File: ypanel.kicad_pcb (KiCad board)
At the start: 6 copper layers, 64 x 58 mm, 57 parts, among them IC2 TSL2561, J1 XF2M-1015-1A, J2 U.FL-R-SMT-1, J3 BATTERY CONNECTOR, J4 B2B-PH-SM4-TB_LF__SN_, U1 SWLP.12.B, U2 Value, U3 SW_SPDT, U4 SW_SPDT

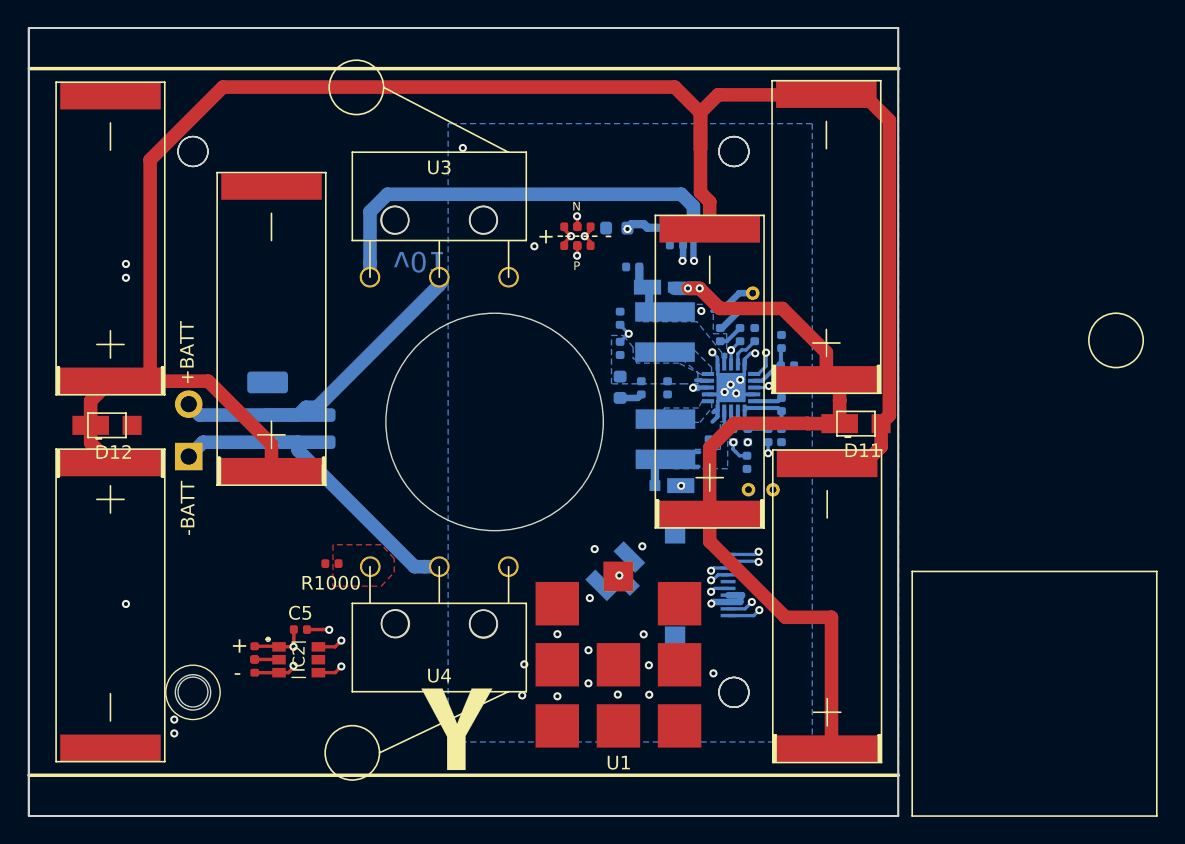
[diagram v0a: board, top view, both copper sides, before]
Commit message: Added new antenna to -Y
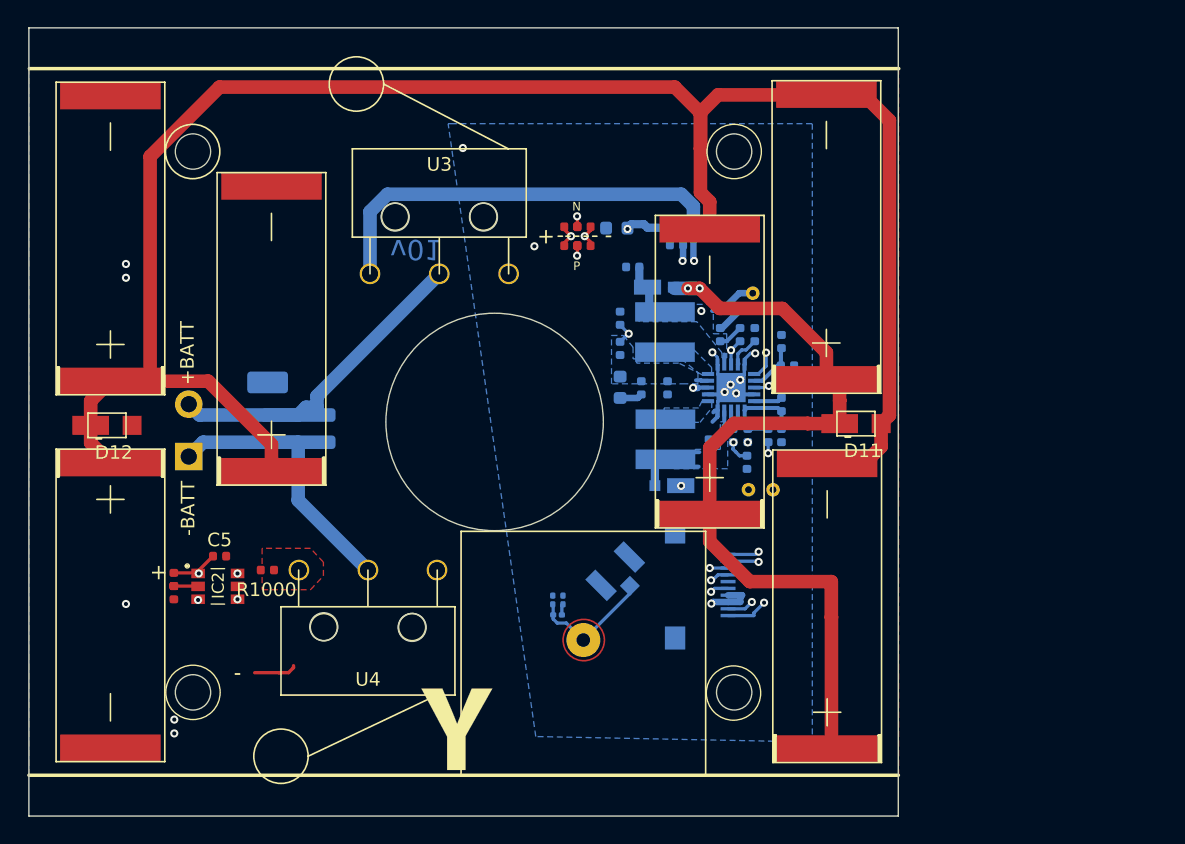
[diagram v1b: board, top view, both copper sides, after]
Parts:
- removed U1: SWLP.12.B, custom-footprints:SWLP-12-B
- added AE1: SXP.18.4.A.02, ypanel:SXP.18.4.A.02, F.Cu at (153.8, 115.0)
- added C12: TBD, Capacitor_SMD:C_0201_0603Metric, B.Cu at (152.3, 112.1)
- added C13: TBD, Capacitor_SMD:C_0201_0603Metric, B.Cu at (151.6, 112.1)
- added L3: TBD, Inductor_SMD:L_0201_0603Metric, B.Cu at (151.9, 113.2)
- moved IC2 8.04 mm to (126.9, 111.1)
- moved C5 8.04 mm to (127.0, 108.9)
- moved R17 8.04 mm to (123.7, 110.6)
- moved R18 8.04 mm to (123.7, 111.6)
- moved U4 5.26 mm to (137.9, 109.9)
- moved R1000 4.77 mm to (130.6, 109.9)
- moved U3 0.25 mm to (143.2, 88.1)
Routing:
- net +3V3: track 53.5 -> 62.1 mm
- net Net-(AE1-Pad1): track 1.08 -> 9.36 mm, vias 1 -> 0
- net SDA1: track 32.8 -> 40.7 mm
- net SCL1: track 33.1 -> 40.4 mm
- net Net-(J3-Pad1): track 23.0 -> 20.0 mm
- net GND: track 22.4 -> 20.8 mm, vias 26 -> 11
- net /VSOLAR_FULL: track 59.8 -> 61.3 mm
- net COIL_P: track 49.1 -> 50.4 mm
- net Net-(C12-Pad1): track 0.00 -> 0.81 mm
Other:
- outline, holes or cut-outs redrawn

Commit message: updated 3d footprint paths and generated new step file
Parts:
- J2: value U.FL-R-SMT-1 -> Conn_Coaxial
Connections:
- J2 pad 1: GND -> Net-(C12-Pad1)
- J2 pad 3: Net-(AE1-Pad1) -> (no net)
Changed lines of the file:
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@@
-(kicad_pcb (version 20171130) (host pcbnew "(5.1.4-0-10_14)")
+(kicad_pcb (version 20171130) (host pcbnew 5.0.2-bee76a0~70~ubuntu18.04.1)
   (general
     (thickness 1.6)
@@
     (3 In3.Cu signal hide)
     (4 In4.Cu signal hide)
-    (31 Bottom signal hide)
+    (31 Bottom signal)
     (32 B.Adhes user hide)
     (33 F.Adhes user hide)
@@
   )
   (setup
-    (last_trace_width 1)
+    (last_trace_width 0.127)
     (user_trace_width 0.127)
     (user_trace_width 0.16)
@@
     (zone_45_only yes)
     (trace_min 0.127)
+    (segment_width 0.2)
+    (edge_width 0.05)
     (via_size 0.6)
     (via_drill 0.3)
@@
     (uvia_min_size 0.2)
     (uvia_min_drill 0.1)
-    (edge_width 0.05)
-    (segment_width 0.2)
     (pcb_text_width 0.3)
     (pcb_text_size 1.5 1.5)
@@
     (uvia_dia 0.3)
     (uvia_drill 0.1)
+    (diff_pair_gap 0.1524)
     (diff_pair_width 0.1524)
-    (diff_pair_gap 0.1524)
     (add_net +3V3)
     (add_net /VBAT)
@@
     (pad 1 thru_hole circle (at 0 0) (size 2.5 2.5) (drill 1) (layers Bottom B.Mask)
       (net 31 "Net-(AE1-Pad1)") (solder_mask_margin 0.5) (clearance 0.5))
-    (model ${CUSTOM_FOOTPRINT_DIR}/3d/SXP.18.4.A.02.step
+    (model ${SPACECRAFT_LIB_DIR}/3d/SXP.18.4.A.02.step
       (offset (xyz 1 0 4))
       (scale (xyz 1 1 1))
@@
     (pad 10 smd rect (at -2.25 0 90) (size 0.25 1.1) (layers Bottom B.Paste B.Mask)
       (net 19 COIL_P))
-    (model ${CUSTOM_FOOTPRINT_DIR}/3d/XF2M-1015-1A.stp
+    (model ${SPACECRAFT_LIB_DIR}/3d/XF2M-1015-1A.stp
       (offset (xyz 0 -5 0))
       (scale (xyz 1 1 1))
@@
     (pad 1 smd rect (at -1.2 0) (size 2.7 1.4) (layers Top F.Paste F.Mask)
       (net 1 "Net-(D11-Pad2)"))
+    (model ${KISYS3DMOD}/Diode_SMD.3dshapes/D_PowerDI-123.step
+      (at (xyz 0 0 0))
+      (scale (xyz 1 1 1))
+      (rotate (xyz 0 0 0))
+    )
   )
   (module "SolarCellParts:SB Diode" (layer Top)
@@
     (pad 1 smd rect (at -1.2 0) (size 2.7 1.4) (layers Top F.Paste F.Mask)
       (net 28 /VSOLAR_FULL))
+    (model ${KISYS3DMOD}/Diode_SMD.3dshapes/D_PowerDI-123.step
+      (at (xyz 0 0 0))
+      (scale (xyz 1 1 1))
+      (rotate (xyz 0 0 0))
+    )
   )
   (module custom-footprints:KXOB25-05X3F (layer Top)
@@
     (pad 1 smd rect (at 0 0 90) (size 2 7.4) (layers Top F.Paste F.Mask)
       (net 28 /VSOLAR_FULL))
-    (model "${CUSTOM_FOOTPRINT_DIR}/3d/KXOB22-12X1F .step"
-      (offset (xyz 10.4902 0.0508 0))
-      (scale (xyz 1.04 1.1 1))
+    (model ${SPACECRAFT_LIB_DIR}/3d/SolarCell.STEP
+      (offset (xyz -115.85 45.7 -1.7))
+      (scale (xyz 1 1 1))
       (rotate (xyz 0 0 0))
     )
@@
     (pad 1 smd rect (at -1.45 -0.95 90) (size 0.7 1) (layers Top F.Paste F.Mask)
       (net 6 +3V3))
-    (model ${CUSTOM_FOOTPRINT_DIR}/3d/TSL2561.stp
+    (model ${SPACECRAFT_LIB_DIR}/3d/TSL2561.stp
       (at (xyz 0 0 0))
       (scale (xyz 1 1 1))
@@
     (pad 1 smd rect (at 0 0 90) (size 2 7.4) (layers Top F.Paste F.Mask)
       (net 1 "Net-(D11-Pad2)"))
-    (model "${CUSTOM_FOOTPRINT_DIR}/3d/KXOB22-12X1F .step"
-      (offset (xyz 10.4902 0.0508 0))
-      (scale (xyz 1.04 1.1 1))
+    (model ${SPACECRAFT_LIB_DIR}/3d/SolarCell.STEP
+      (offset (xyz -115.85 45.7 -1.7))
+      (scale (xyz 1 1 1))
       (rotate (xyz 0 0 0))
     )
@@
     (pad 1 smd rect (at 0 0 90) (size 2 7.4) (layers Top F.Paste F.Mask)
       (net 28 /VSOLAR_FULL))
-    (model "${CUSTOM_FOOTPRINT_DIR}/3d/KXOB22-12X1F .step"
-      (offset (xyz 10.4902 0.0508 0))
-      (scale (xyz 1.04 1.1 1))
+    (model ${SPACECRAFT_LIB_DIR}/3d/SolarCell.STEP
+      (offset (xyz -115.85 45.7 -1.7))
+      (scale (xyz 1 1 1))
       (rotate (xyz 0 0 0))
     )
@@
     (pad 1 smd rect (at 0 0 90) (size 2 7.4) (layers Top F.Paste F.Mask)
       (net 1 "Net-(D11-Pad2)"))
-    (model "${CUSTOM_FOOTPRINT_DIR}/3d/KXOB22-12X1F .step"
-      (offset (xyz 10.4902 0.0508 0))
-      (scale (xyz 1.04 1.1 1))
+    (model ${SPACECRAFT_LIB_DIR}/3d/SolarCell.STEP
+      (offset (xyz -115.85 45.7 -1.7))
+      (scale (xyz 1 1 1))
       (rotate (xyz 0 0 0))
     )
@@
     (pad 1 smd rect (at 0 0 270) (size 2 7.4) (layers Top F.Paste F.Mask)
       (net 1 "Net-(D11-Pad2)"))
-    (model "${CUSTOM_FOOTPRINT_DIR}/3d/KXOB22-12X1F .step"
-      (offset (xyz 10.4902 0.0508 0))
-      (scale (xyz 1.04 1.1 1))
+    (model ${SPACECRAFT_LIB_DIR}/3d/SolarCell.STEP
+      (offset (xyz -115.85 45.7 -1.7))
+      (scale (xyz 1 1 1))
       (rotate (xyz 0 0 0))
     )
@@
     (pad 1 smd rect (at 0 0 90) (size 2 7.4) (layers Top F.Paste F.Mask)
       (net 28 /VSOLAR_FULL))
-    (model "${CUSTOM_FOOTPRINT_DIR}/3d/KXOB22-12X1F .step"
-      (offset (xyz 10.4902 0.0508 0))
-      (scale (xyz 1.04 1.1 1))
+    (model ${SPACECRAFT_LIB_DIR}/3d/SolarCell.STEP
+      (offset (xyz -115.85 45.7 -1.7))
+      (scale (xyz 1 1 1))
       (rotate (xyz 0 0 0))
     )
@@
     (pad 2 smd rect (at 1.25 0 270) (size 0.8 0.8) (layers Bottom B.Paste B.Mask)
       (net 28 /VSOLAR_FULL))
+    (model ${KISYS3DMOD}/Diode_SMD.3dshapes/D_SOD-323.step
+      (at (xyz 0 0 0))
+      (scale (xyz 1 1 1))
+      (rotate (xyz 0 0 0))
+    )
   )
   (module Resistor_SMD:R_0402_1005Metric (layer Top)
@@
       (effects (font (size 1.27 1.27) (thickness 0.254)) (justify mirror))
     )
-    (fp_text value U.FL-R-SMT-1 (at -1.09467 2.881 45) (layer B.SilkS) hide
+    (fp_text value Conn_Coaxial (at -1.09467 2.881 45) (layer B.SilkS) hide
       (effects (font (size 1.27 1.27) (thickness 0.254)) (justify mirror))
     )
@@
       (effects (font (size 1.27 1.27) (thickness 0.254)) (justify mirror))
     )
-    (pad 3 smd rect (at 0 -1.525 135) (size 1.05 1.05) (layers Bottom B.Paste B.Mask)
-      (net 31 "Net-(AE1-Pad1)"))
+    (pad 3 smd rect (at 0 -1.525 135) (size 1.05 1.05) (layers Bottom B.Paste B.Mask))
     (pad 2 smd rect (at 1.475001 0 225) (size 1.05 2.25) (layers Bottom B.Paste B.Mask)
       (net 2 GND))
     (pad 1 smd rect (at -1.475001 0 225) (size 1.05 2.25) (layers Bottom B.Paste B.Mask)
-      (net 2 GND))
-    (model ${CUSTOM_FOOTPRINT_DIR}/3d/U.FL-R-SMT-1.stp
+      (net 32 "Net-(C12-Pad1)"))
+    (model ${SPACECRAFT_LIB_DIR}/3d/U.FL-R-SMT-1.stp
       (offset (xyz 55.2 1 22.5))
       (scale (xyz 1 1 1))
@@
     (pad 1 smd rect (at -1.7 1 180) (size 0.3 0.9) (layers Bottom B.Paste B.Mask)
       (net 2 GND))
-    (model ${CUSTOM_FOOTPRINT_DIR}/3d/BQ25570RGRR.stp
+    (model ${SPACECRAFT_LIB_DIR}/3d/BQ25570RGRR.stp
       (at (xyz 0 0 0))
       (scale (xyz 1 1 1))
@@
     (pad 1 smd rect (at -0.65 0 90) (size 1.1 2) (layers Bottom B.Paste B.Mask)
       (net 6 +3V3))
+    (model ${KISYS3DMOD}/Diode_SMD.3dshapes/D_SOD-323.step
+      (at (xyz 0 0 0))
+      (scale (xyz 1 1 1))
+      (rotate (xyz 0 0 0))
+    )
   )
   (module Resistor_SMD:R_0402_1005Metric (layer Bottom)

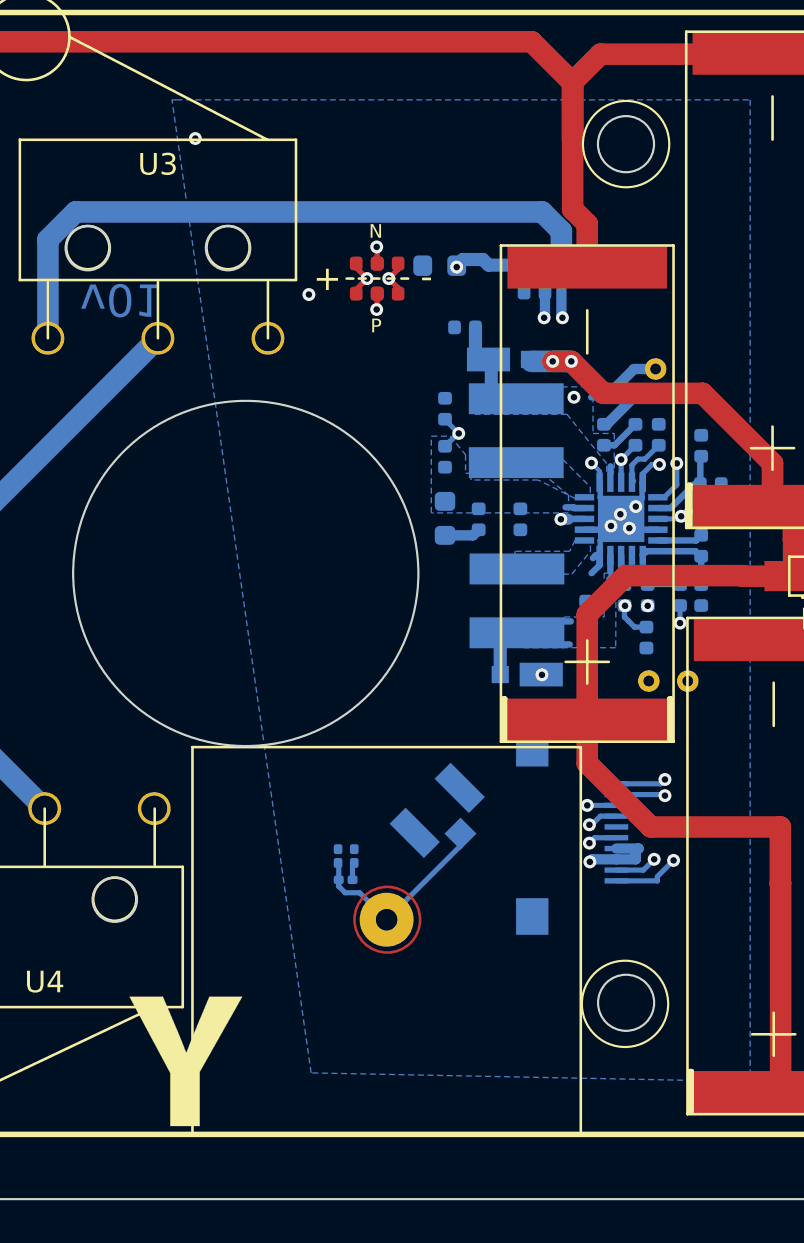
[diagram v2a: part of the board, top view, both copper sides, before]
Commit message: fixed antenna footprint and regenerated step file
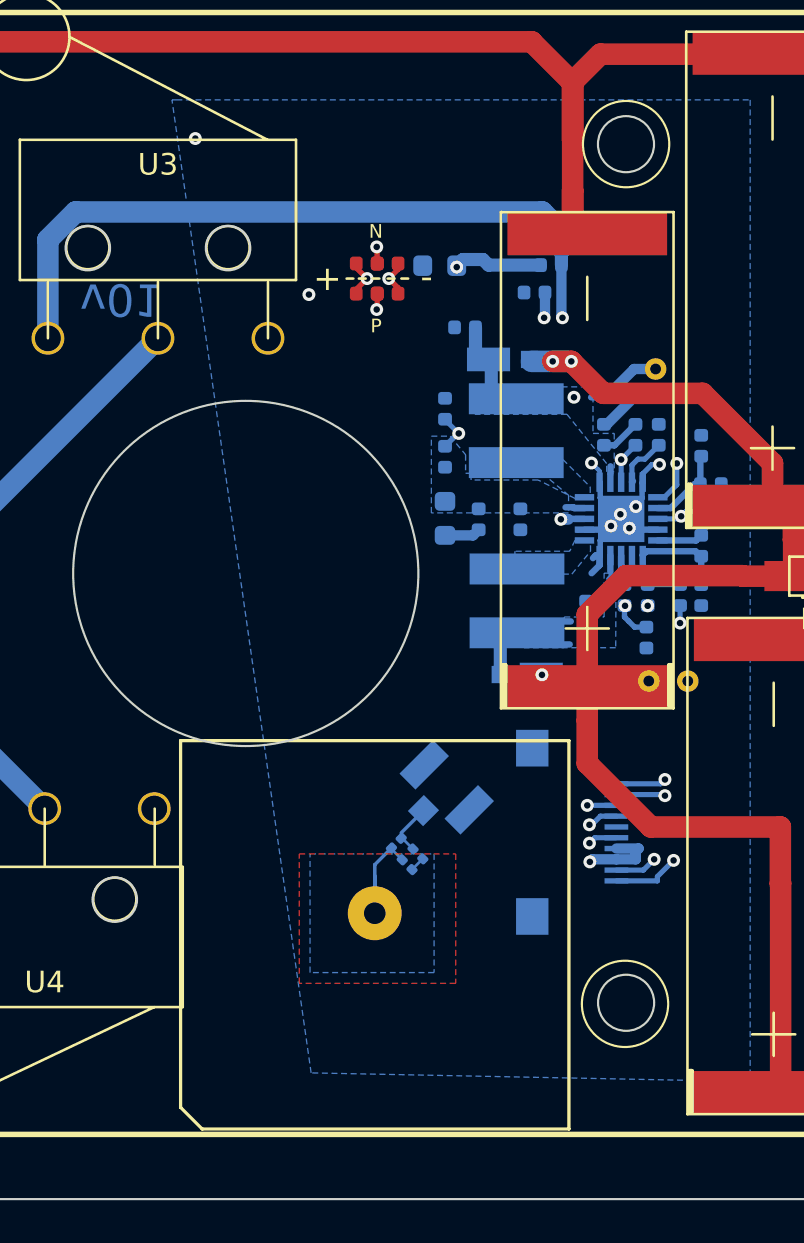
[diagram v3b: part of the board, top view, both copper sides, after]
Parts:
- removed Ref** (x2): Val**, custom-footprints:ypanel
- AE1: footprint ypanel:SXP.18.4.A.02 -> spacecraft-footprints:SXP.18.4.A.02
- J2: footprint custom-footprints:U.FL-R-SMT-1 -> Connector_Coaxial:U.FL_Hirose_U.FL-R-SMT-1_Vertical
- moved C13 3.22 mm to (154.8, 112.5), turned to 315 degrees
- moved C12 2.95 mm to (155.2, 112.0), turned to 315 degrees
- moved L3 2.90 mm to (154.2, 111.5), turned to 45 degrees
- moved SC3 1.55 mm to (163.1, 104.2)
- moved AE1 0.89 mm to (153.2, 115.8), turned to 180 degrees
- moved J2 0.74 mm to (156.2, 109.2), turned to 45 degrees
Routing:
- net Net-(AE1-Pad1): track 9.36 -> 6.35 mm
- net Net-(C12-Pad1): track 0.81 -> 1.86 mm
- net GND: track 20.8 -> 21.5 mm
- net Net-(D11-Pad2): track 137.1 -> 136.4 mm

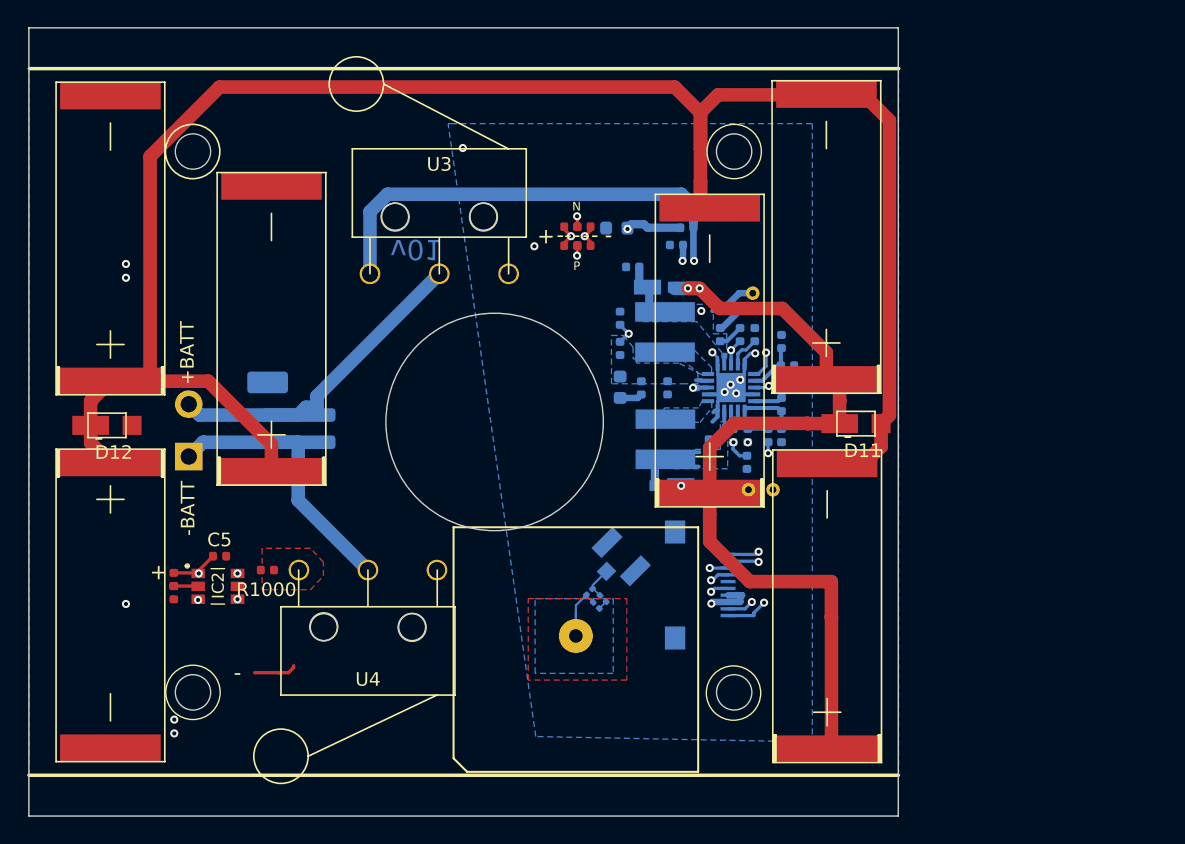
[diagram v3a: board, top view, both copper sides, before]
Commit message: moved camera hole and other components
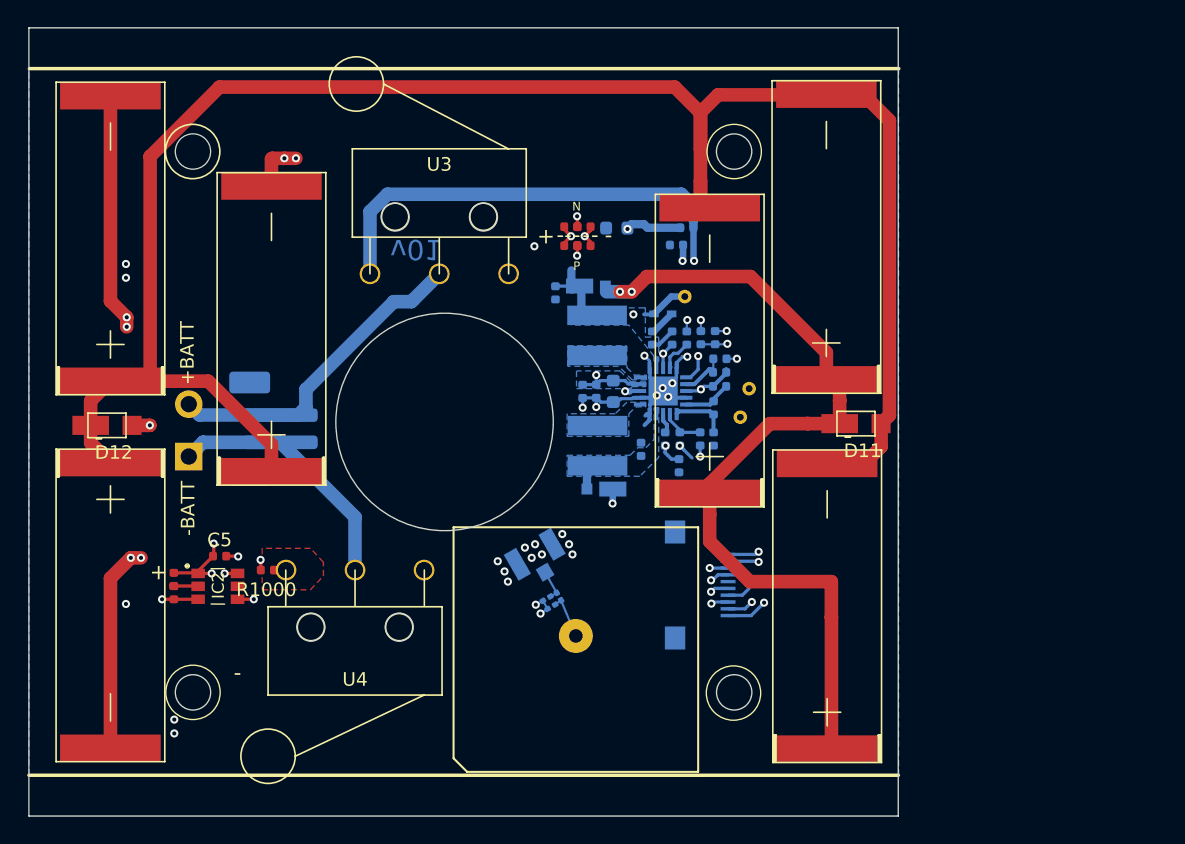
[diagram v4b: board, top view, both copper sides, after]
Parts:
- moved TP2 7.65 mm to (166.0, 96.5)
- moved R12 7.14 mm to (163.5, 92.8)
- moved R13 6.00 mm to (162.4, 92.8), turned to 270 degrees
- moved C2 5.99 mm to (151.8, 89.5), turned to 270 degrees
- moved J2 5.79 mm to (150.5, 109.1), turned to 120 degrees
- moved TP1 5.37 mm to (165.3, 98.7)
- moved C8 5.25 mm to (154.8, 96.7)
- moved R2 5.02 mm to (163.8, 95.3)
- moved L2 5.02 mm to (154.8, 100.8)
- moved C1 5.01 mm to (160.8, 102.2)
- moved C3 5.01 mm to (158.9, 92.8)
- moved C4 5.01 mm to (161.4, 92.8)
- moved C7 5.01 mm to (158.0, 101.0)
- moved D1 5.01 mm to (159.6, 91.0)
- moved D2 5.01 mm to (155.3, 103.9)
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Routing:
- net GND: track 21.5 -> 68.8 mm, vias 11 -> 36
- net Net-(C11-Pad1): track 0.89 -> 16.6 mm, vias 0 -> 2
- net /VSOLAR_FULL: track 61.3 -> 65.6 mm
- net Net-(C7-Pad1): track 5.20 -> 1.94 mm
- net +3V3: track 62.1 -> 65.1 mm, vias 3 -> 4
- net Net-(AE1-Pad1): track 6.35 -> 3.37 mm
- net Net-(R11-Pad1): track 11.8 -> 8.98 mm
- net VSOLAR: track 9.21 -> 11.0 mm
- net SCL1: track 40.4 -> 41.7 mm
- net Net-(J3-Pad1): track 20.0 -> 18.9 mm
- net SDA1: track 40.7 -> 41.8 mm
- net /VBAT: track 18.9 -> 18.3 mm
- added copper zone on In4.Cu, net GND
- removed copper zone on F.Cu, net GND
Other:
- outline, holes or cut-outs redrawn
